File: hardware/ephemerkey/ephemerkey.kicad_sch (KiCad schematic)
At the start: 0 parts

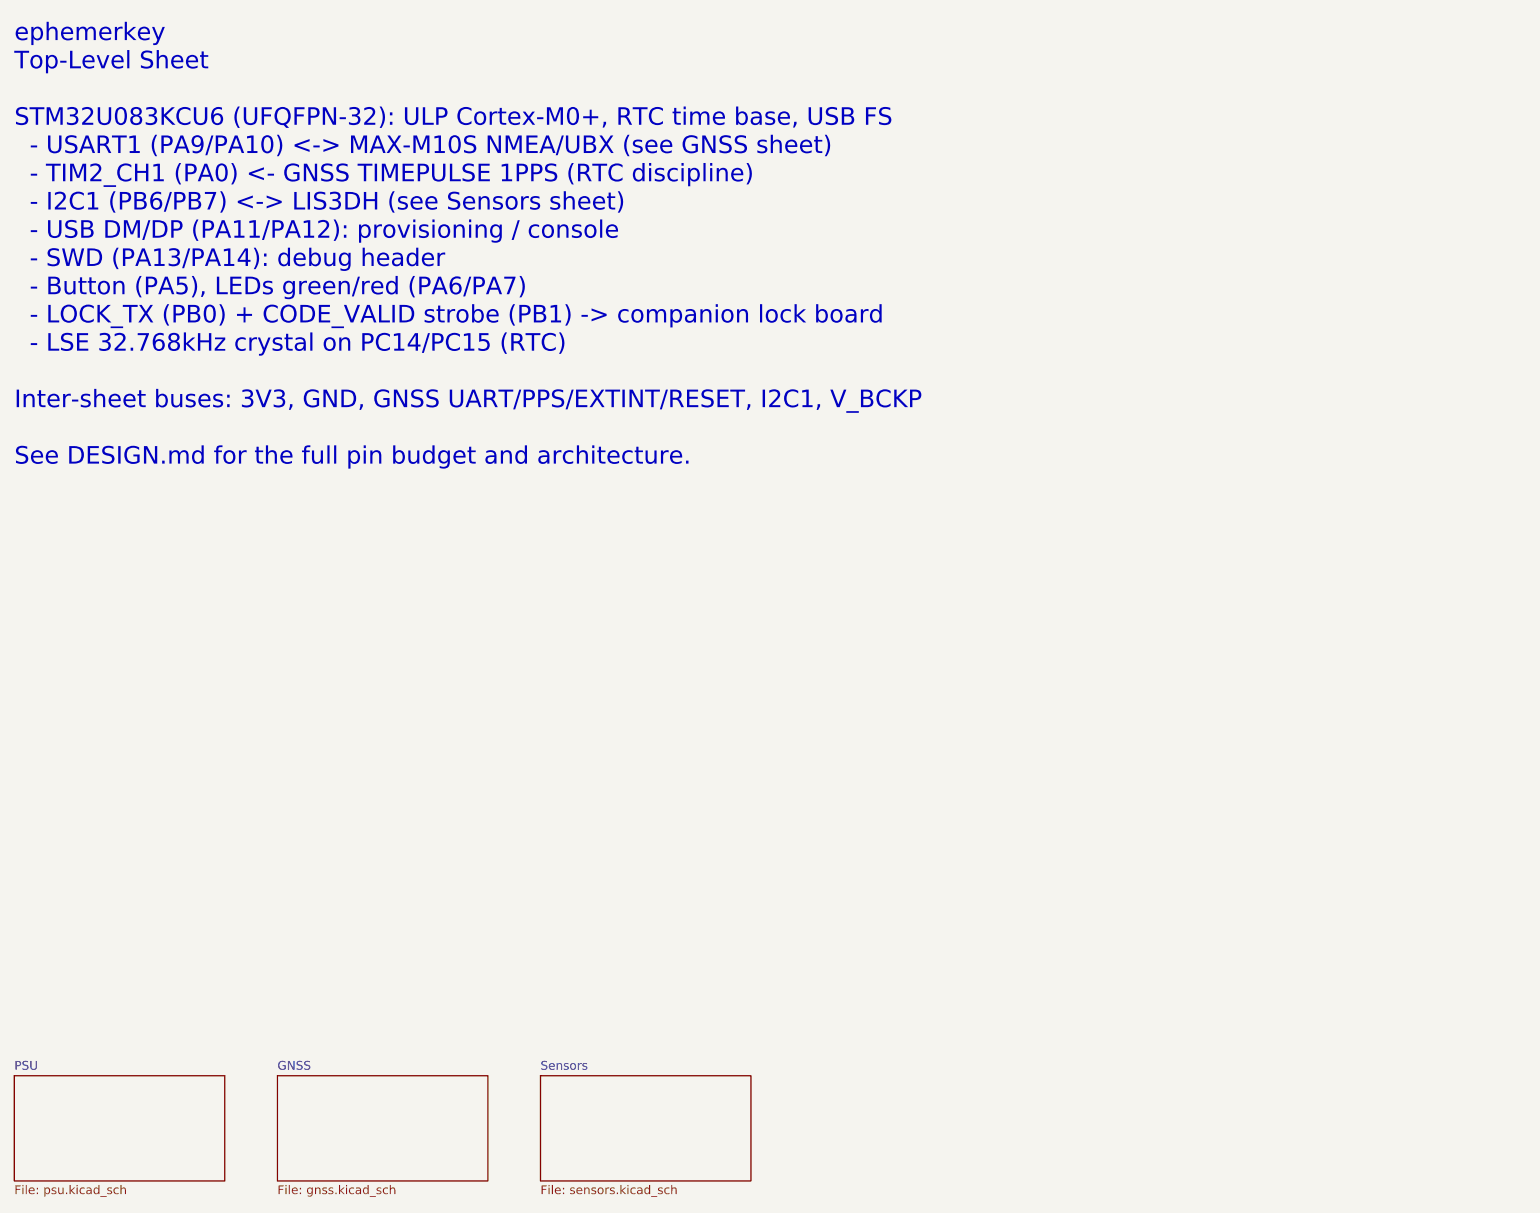
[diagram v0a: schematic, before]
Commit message: Populate schematic sheets per subsystem (placed, not wired)
Adopt the house schgen workflow (kschgen.py + manifest), matching notchdeck/
tsumikoro: schematic is GENERATED from scripts/ephemerkey.schgen.py, parts
PLACED with per-sheet on-canvas wiring notes; wiring is the next eeschema phase.

57 components across MCU / PSU / GNSS / Sensors, every line on a real KiCad
bundled symbol+footprint and a JLCPCB LCSC (0402 passives, 0805 bulk):
- MCU: STM32U083KCU6, 32.768kHz LSE crystal (C32346) + 12pF loads, SWD TC2030,
  lock-out header, decoupling, BOOT0/NRST, button, status LEDs.
- PSU: USB-C (GCT USB4105) + USBLC6 ESD + 5.1k CC, MCP73831 charger (Rprog 4.7k
  ~213mA for 500mAh), AO3401A load-share + B5819W, TPS63900 + FNR3015 2.2µH
  (small) + 10µF caps, JST-PH RA battery (S2B-PH-K-S).
- GNSS: MAX-M10S + W3011A + pi-match (series 0R, shunts DNP), VCC_RF ferrite,
  V_BCKP/V_IO/VCC decoupling.
- Sensors: LIS3DH + decoupling + 4.7k I2C pull-ups.

Tooling: kschgen.py, kicad-sch-check.py, kicad-sch-render.sh; Makefile gen/
check/render targets. make check: 57 comps, 57/57 footprints, no dup refs.
Added hardware/PARTS.md (BOM source of truth). CLAUDE.md documents the workflow.

Co-Authored-By: Claude Opus 4.8 (1M context) <noreply@anthropic.com>
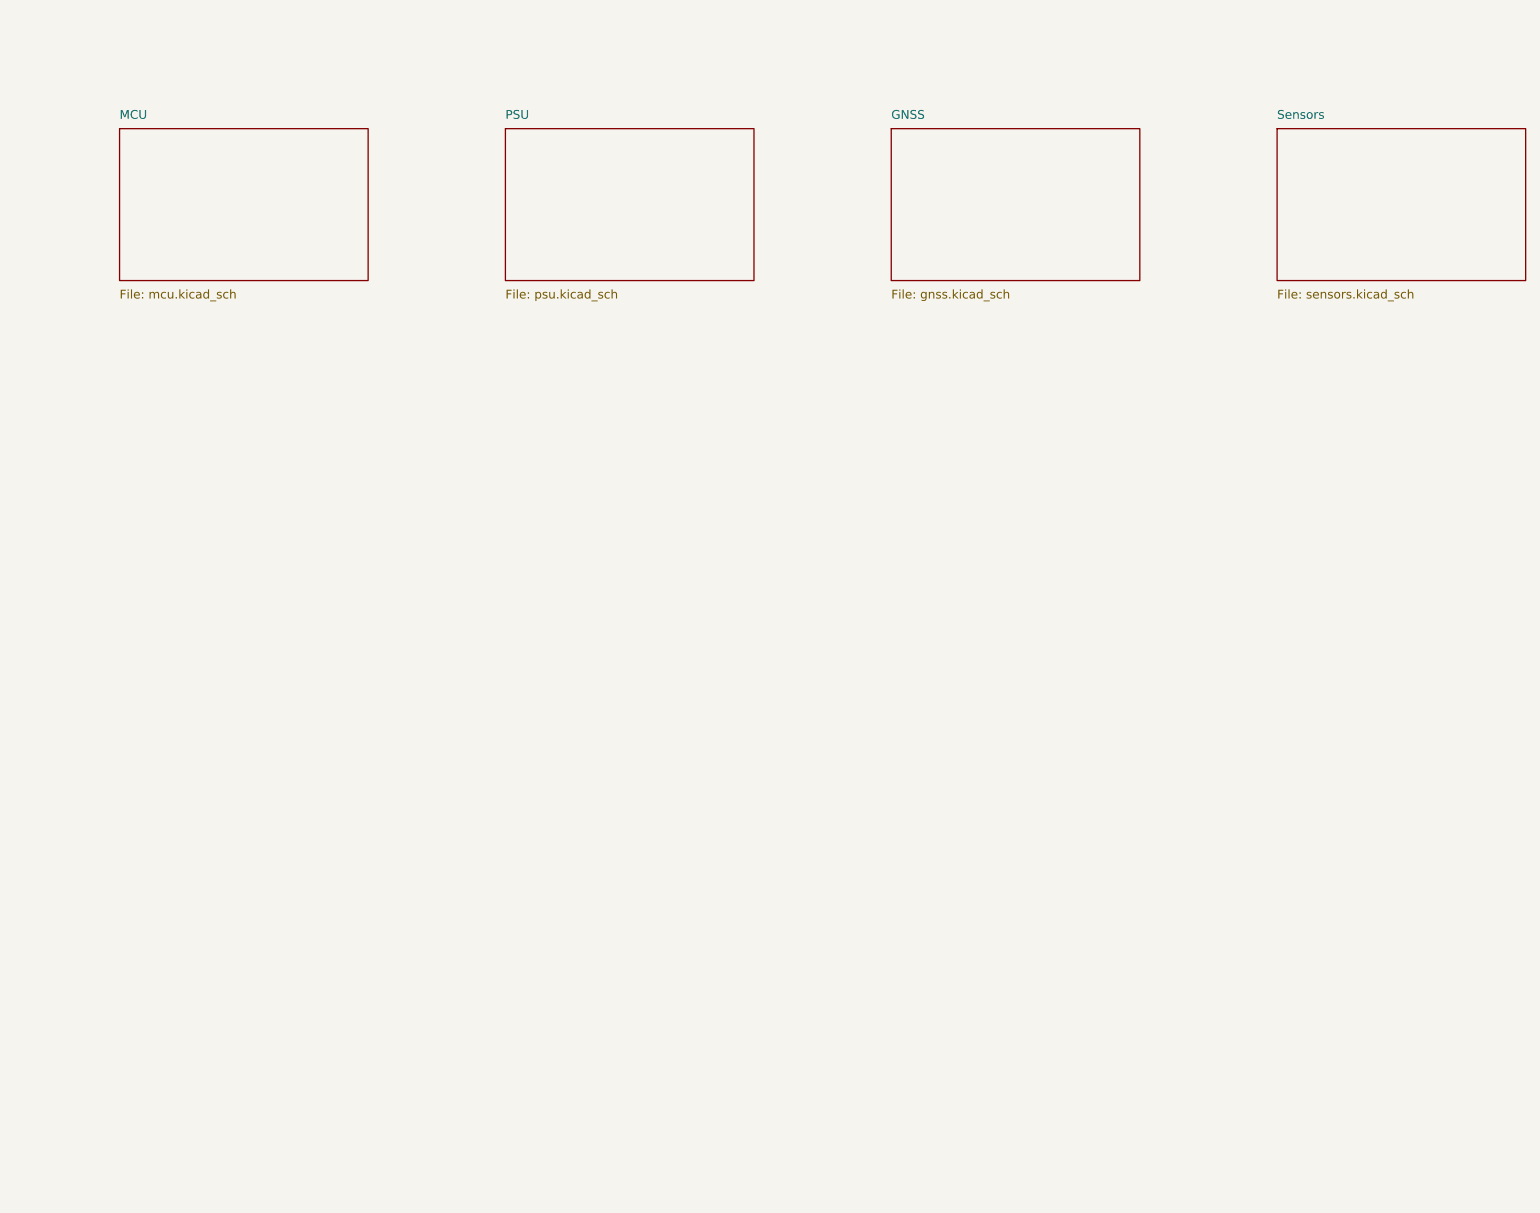
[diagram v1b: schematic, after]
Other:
- added sheet MCU (mcu.kicad_sch)
- note removed: "ephemerkey Top-Level Sheet STM32U083KCU6 (UFQFPN-32): ULP Cortex-M0+, RTC time base, USB FS - USART1 (PA9/PA10) <-> MAX-M10S NMEA/UBX (see GNSS sheet) - TIM2_CH1 (PA0) <- GNSS TIMEPULSE 1PPS (RTC discipline) - I2C1 (PB6/PB7) <-> LIS3DH (see Sensors sheet) - USB DM/DP (PA11/PA12): provisioning / console - SWD (PA13/PA14): debug header - Button (PA5), LEDs green/red (PA6/PA7) - LOCK_TX (PB0) + CODE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"
- company: (none) -> EphemerKey Authors
- title: ephemerkey — Main -> ephemerkey
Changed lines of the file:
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@@
 	(paper "A3")
 	(title_block
-		(title "ephemerkey — Main")
+		(title "ephemerkey")
 		(date "2026-06-21")
 		(rev "0.1")
-		(comment 1 "STM32U083KCU6 + MAX-M10S GNSS + LIS3DH + TPS63900")
-		(comment 2 "GPS-geofenced TOTP (RFC 6238) code generator")
-		(comment 3 "CERN-OHL-P v2 / Apache 2.0")
-		(comment 4 "EphemerKey Authors")
+		(company "EphemerKey Authors")
+		(comment 1 "GPS-geofenced TOTP (RFC 6238) generator")
+		(comment 2 "Top-level — hierarchical sheets per subsystem")
 	)
-	(text "ephemerkey\nTop-Level Sheet\n\nSTM32U083KCU6 (UFQFPN-32): ULP Cortex-M0+, RTC time base, USB FS\n  - USART1 (PA9/PA10) <-> MAX-M10S NMEA/UBX (see GNSS sheet)\n  - TIM2_CH1 (PA0) <- GNSS TIMEPULSE 1PPS (RTC discipline)\n  - I2C1 (PB6/PB7) <-> LIS3DH (see Sensors sheet)\n  - USB DM/DP (PA11/PA12): provisioning / console\n  - SWD (PA13/PA14): debug header\n  - Button (PA5), LEDs green/red (PA6/PA7)\n  - LOCK_TX (PB0) + CODE_VALID strobe (PB1) -> companion lock board\n  - LSE 32.768kHz crystal on PC14/PC15 (RTC)\n\nInter-sheet buses: 3V3, GND, GNSS UART/PPS/EXTINT/RESET, I2C1, V_BCKP\n\nSee DESIGN.md for the full pin budget and architecture."
-		(exclude_from_sim no)
-		(at 25.4 25.4 0)
-		(effects
-			(font
-				(size 2.54 2.54)
-			)
-			(justify left top)
+	(sheet
+		(at 40.64 40.64)
+		(size 36.00 22.00)
+		(fields_autoplaced yes)
+		(stroke (width 0.1524) (type solid))
+		(fill (color 0 0 0 0.0000))
+		(property "Sheetname" "MCU"
+			(at 40.64 39.37 0)
+			(effects (font (size 1.27 1.27)) (justify left bottom))
+		)
+		(property "Sheetfile" "mcu.kicad_sch"
+			(at 40.64 63.91 0)
+			(effects (font (size 1.27 1.27)) (justify left top))
 		)
 	)
 	(sheet
-		(at 25.4 177.8)
-		(size 30.48 15.24)
-		(exclude_from_sim no)
-		(in_bom yes)
-		(on_board yes)
-		(dnp no)
+		(at 96.52 40.64)
+		(size 36.00 22.00)
 		(fields_autoplaced yes)
-		(stroke
-			(width 0.1524)
-			(type solid)
-		)
-		(fill
-			(color 255 255 225 1)
-		)
+		(stroke (width 0.1524) (type solid))
+		(fill (color 0 0 0 0.0000))
 		(property "Sheetname" "PSU"
-			(at 25.4 177.0884 0)
-			(show_name no)
-			(do_not_autoplace no)
-			(effects
-				(font
-					(size 1.27 1.27)
-				)
-				(justify left bottom)
-			)
+			(at 96.52 39.37 0)
+			(effects (font (size 1.27 1.27)) (justify left bottom))
 		)
 		(property "Sheetfile" "psu.kicad_sch"
-			(at 25.4 193.6146 0)
-			(show_name no)
-			(do_not_autoplace no)
-			(effects
-				(font
-					(size 1.27 1.27)
-				)
-				(justify left top)
-			)
+			(at 96.52 63.91 0)
+			(effects (font (size 1.27 1.27)) (justify left top))
 		)
 	)
 	(sheet
-		(at 63.5 177.8)
-		(size 30.48 15.24)
-		(exclude_from_sim no)
-		(in_bom yes)
-		(on_board yes)
-		(dnp no)
+		(at 152.40 40.64)
+		(size 36.00 22.00)
 		(fields_autoplaced yes)
-		(stroke
-			(width 0.1524)
-			(type solid)
-		)
-		(fill
-			(color 225 255 225 1)
-		)
+		(stroke (width 0.1524) (type solid))
+		(fill (color 0 0 0 0.0000))
 		(property "Sheetname" "GNSS"
-			(at 63.5 177.0884 0)
-			(show_name no)
-			(do_not_autoplace no)
-			(effects
-				(font
-					(size 1.27 1.27)
-				)
-				(justify left bottom)
-			)
+			(at 152.40 39.37 0)
+			(effects (font (size 1.27 1.27)) (justify left bottom))
 		)
 		(property "Sheetfile" "gnss.kicad_sch"
-			(at 63.5 193.6146 0)
-			(show_name no)
-			(do_not_autoplace no)
-			(effects
-				(font
-					(size 1.27 1.27)
-				)
-				(justify left top)
-			)
+			(at 152.40 63.91 0)
+			(effects (font (size 1.27 1.27)) (justify left top))
 		)
 	)
 	(sheet
-		(at 101.6 177.8)
-		(size 30.48 15.24)
-		(exclude_from_sim no)
-		(in_bom yes)
-		(on_board yes)
-		(dnp no)
+		(at 208.28 40.64)
+		(size 36.00 22.00)
 		(fields_autoplaced yes)
-		(stroke
-			(width 0.1524)
-			(type solid)
-		)
-		(fill
-			(color 225 235 255 1)
-		)
+		(stroke (width 0.1524) (type solid))
+		(fill (color 0 0 0 0.0000))
 		(property "Sheetname" "Sensors"
-			(at 101.6 177.0884 0)
-			(show_name no)
-			(do_not_autoplace no)
-			(effects
-				(font
-					(size 1.27 1.27)
-				)
-				(justify left bottom)
-			)
+			(at 208.28 39.37 0)
+			(effects (font (size 1.27 1.27)) (justify left bottom))
 		)
 		(property "Sheetfile" "sensors.kicad_sch"
-			(at 101.6 193.6146 0)
-			(show_name no)
-			(do_not_autoplace no)
-			(effects
-				(font
-					(size 1.27 1.27)
-				)
-				(justify left top)
-			)
+			(at 208.28 63.91 0)
+			(effects (font (size 1.27 1.27)) (justify left top))
 		)
 	)
